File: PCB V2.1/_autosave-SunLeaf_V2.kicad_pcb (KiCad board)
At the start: 4 copper layers, 80 x 40 mm, 119 parts, among them IC1 ESP_09, J1 20021121-00010C4LF, J10 B4B-PH-K-S(LF)(SN), J11 B4B-PH-K-S(LF)(SN), J12 B4B-PH-K-S(LF)(SN), J13 B4B-PH-K-S(LF)(SN), J14 B4B-PH-K-S(LF)(SN), J15 B4B-PH-K-S(LF)(SN), J16 B4B-PH-K-S(LF)(SN), J2 0475890001-MicroUSBPort, J3 B2B-PH-K-S(LF)(SN), J4 B3B-PH-K-S(LF)(SN), J5 B4B-PH-K-S(LF)(SN), J6 B4B-PH-K-S(LF)(SN), J7 B4B-PH-K-S(LF)(SN), J8 B4B-PH-K-S(LF)(SN), J9 B4B-PH-K-S(LF)(SN), P1 CONN_01X04, Q1 DMG2307L-7, Q2 DMG2307L-7, SW1 B3U-1000P, SW2 B3U-1000P, T1 1909763-1, U1 STM32F446RET6_-_TQFP64, U2 BQ24210DQCT, U3 AZ1117CR-3.3TRG1_1, U4 74HC4052D, U5 PCA9518DBQR, X1 ABM3B8.000MHZB2T, X2 ABS07-32.768KHZ-9-T

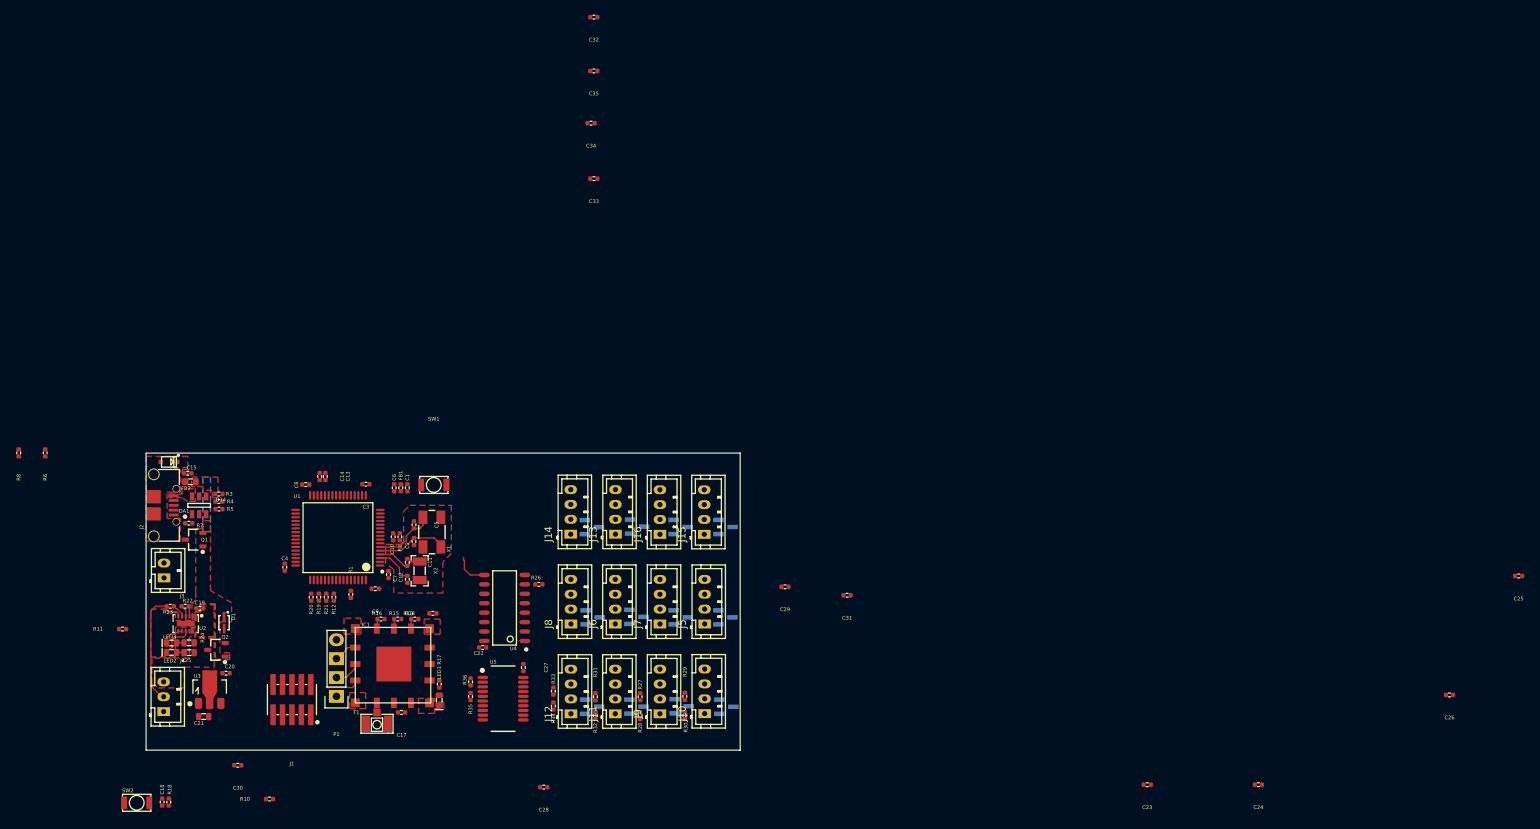
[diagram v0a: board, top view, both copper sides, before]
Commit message: Placement near completeq
placement is near complete, saving as revision, remember KiCAD=crash
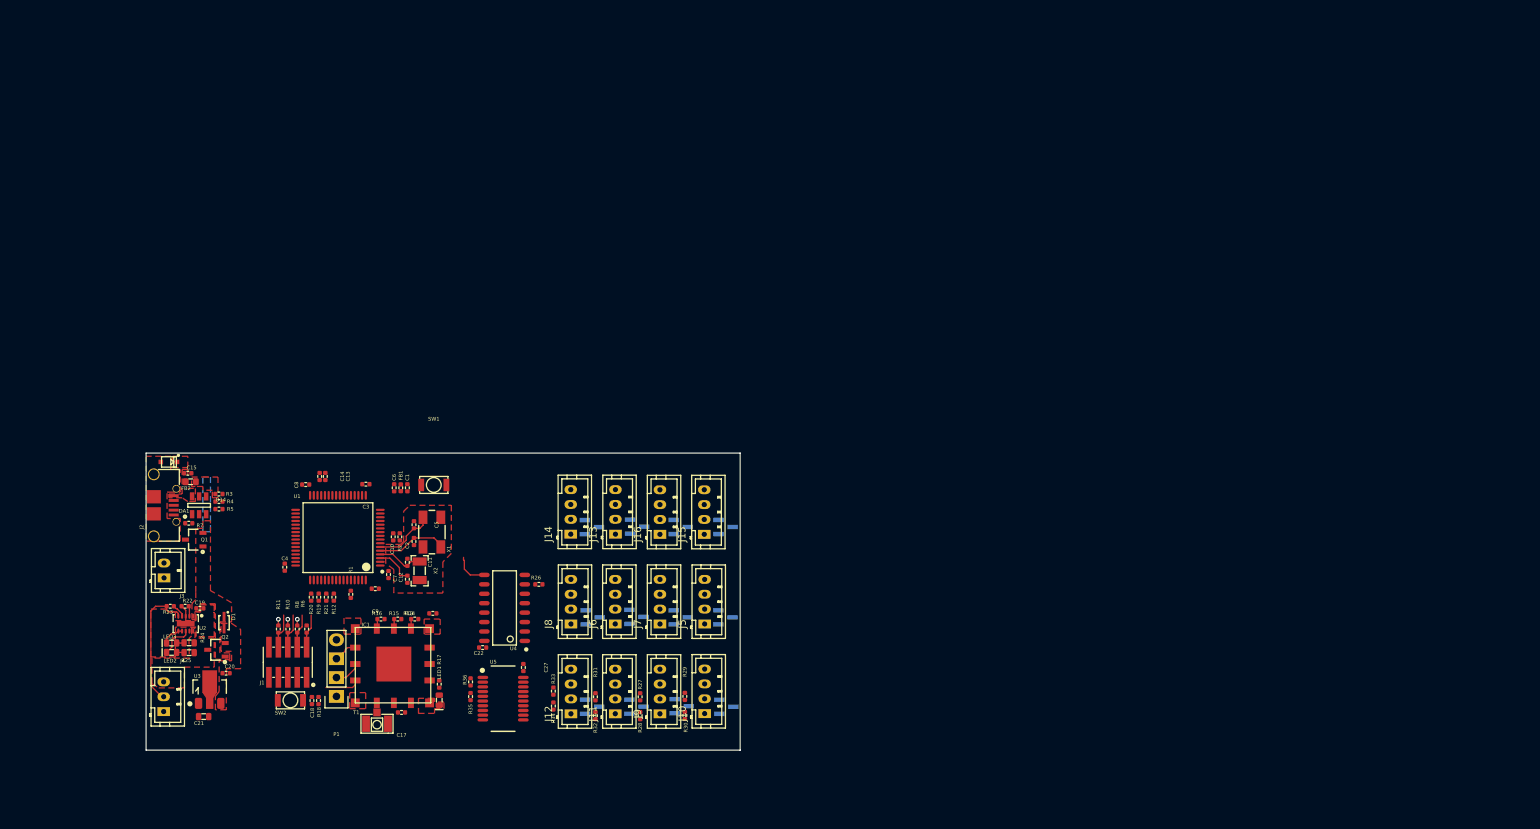
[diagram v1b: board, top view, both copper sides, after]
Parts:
- removed C23, C24, C25, C26, C28, C29, C30, C31, C32, C33, C34, C35: CL05B104JP5NNNC, PCB_Footprints:C0402
- moved R8 44.4 mm to (60.4, 53.7), turned to 270 degrees
- moved R6 42.5 mm to (61.6, 53.7), turned to 270 degrees
- moved SW2 24.9 mm to (59.4, 63.3)
- moved C18 24.4 mm to (62.3, 63.3)
- moved R18 24.4 mm to (63.2, 63.3)
- moved R10 23.0 mm to (59.1, 53.7), turned to 270 degrees
- moved R11 21.0 mm to (57.8, 53.7), turned to 270 degrees
- moved J1 5.06 mm to (59.1, 58.2)
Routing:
- net /MCU-STM32F446RET6/SWO_TDO: track 0.00 -> 4.87 mm
- net /MCU-STM32F446RET6/SWO_TDI: track 0.00 -> 4.85 mm
- net /MCU-STM32F446RET6/SWCLK_TCK: track 0.00 -> 4.59 mm
- net /MCU-STM32F446RET6/SWDIO_TMS: track 0.00 -> 4.57 mm
- net +3V3: track 0.00 -> 2.52 mm, vias 0 -> 3
- added copper zone on F.Cu, net Net-(C20-Pad1)
